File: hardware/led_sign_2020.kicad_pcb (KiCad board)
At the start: 2 copper layers, 70 x 86 mm, 29 parts, among them Q1 STD26P3LLH6, U1 ESP32-DevKitC, U2 MC74VHC1GT125, U3 MC74VHC1GT125, U4 MAX17601, U5 MAX17601, U6 MAX17601, U7 MAX17601

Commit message: no idea what I changed
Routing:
- net /DATA: track 14.3 -> 12.4 mm
- net /EN: track 79.0 -> 80.4 mm
- net /CLK: track 19.2 -> 18.5 mm
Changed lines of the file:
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@@
     (thickness 1.6)
     (drawings 10)
-    (tracks 367)
+    (tracks 364)
     (zones 0)
     (modules 29)
@@
   )
   (setup
-    (last_trace_width 2)
+    (last_trace_width 0.25)
     (user_trace_width 0.25)
     (user_trace_width 0.5)
@@
   (segment (start 120.1 75.4) (end 120.8 76.1) (width 0.25) (layer F.Cu) (net 1))
   (segment (start 118.4 75.4) (end 120.1 75.4) (width 0.25) (layer F.Cu) (net 1))
-  (segment (start 116.65 70.66) (end 116.65 70.15) (width 0.25) (layer F.Cu) (net 1))
-  (segment (start 120.384999 69.984999) (end 120.8 70.4) (width 0.25) (layer F.Cu) (net 1))
-  (segment (start 116.65 70.15) (end 116.815001 69.984999) (width 0.25) (layer F.Cu) (net 1))
-  (segment (start 118.55 70.66) (end 118.55 70.05) (width 0.25) (layer F.Cu) (net 1))
-  (segment (start 118.55 70.05) (end 118.484999 69.984999) (width 0.25) (layer F.Cu) (net 1))
-  (segment (start 118.484999 69.984999) (end 120.384999 69.984999) (width 0.25) (layer F.Cu) (net 1))
-  (segment (start 116.815001 69.984999) (end 118.484999 69.984999) (width 0.25) (layer F.Cu) (net 1))
   (via (at 119.8 76.9) (size 0.8) (drill 0.4) (layers F.Cu B.Cu) (net 1))
   (segment (start 120.6 76.1) (end 119.8 76.9) (width 0.25) (layer F.Cu) (net 1))
@@
   (segment (start 92.7875 76.9875) (end 92.7 76.9) (width 0.25) (layer F.Cu) (net 1))
   (segment (start 96.9 76.9) (end 92.7 76.9) (width 2) (layer B.Cu) (net 1))
-  (segment (start 81.94 79.659994) (end 81.94 84.06) (width 0.5) (layer F.Cu) (net 1))
-  (segment (start 81.94 84.06) (end 81.94 85.53) (width 0.5) (layer F.Cu) (net 1))
-  (segment (start 84.7 76.899994) (end 81.94 79.659994) (width 0.5) (layer F.Cu) (net 1))
+  (segment (start 81.94 79.659994) (end 81.94 84.06) (width 2) (layer F.Cu) (net 1))
+  (segment (start 81.94 84.06) (end 81.94 85.53) (width 2) (layer F.Cu) (net 1))
+  (segment (start 84.7 76.899994) (end 81.94 79.659994) (width 2) (layer F.Cu) (net 1))
   (segment (start 119.799987 76.899987) (end 119.8 76.9) (width 2) (layer B.Cu) (net 1))
   (segment (start 104.900013 76.899987) (end 119.799987 76.899987) (width 2) (layer B.Cu) (net 1))
@@
   (segment (start 114.96 101.66) (end 114.96 110.93) (width 2) (layer B.Cu) (net 1))
   (segment (start 111.6 98.3) (end 114.96 101.66) (width 2) (layer B.Cu) (net 1))
+  (segment (start 116.65 70.15) (end 117 69.8) (width 0.25) (layer F.Cu) (net 1))
+  (segment (start 117 69.8) (end 118.3 69.8) (width 0.25) (layer F.Cu) (net 1))
+  (segment (start 116.65 70.66) (end 116.65 70.15) (width 0.25) (layer F.Cu) (net 1))
+  (segment (start 118.669998 69.8) (end 120.2 69.8) (width 0.25) (layer F.Cu) (net 1))
+  (segment (start 118.55 69.919998) (end 118.669998 69.8) (width 0.25) (layer F.Cu) (net 1))
+  (segment (start 120.2 69.8) (end 120.8 70.4) (width 0.25) (layer F.Cu) (net 1))
+  (segment (start 118.55 70.66) (end 118.55 69.919998) (width 0.25) (layer F.Cu) (net 1))
+  (segment (start 118.3 69.8) (end 118.669998 69.8) (width 0.25) (layer F.Cu) (net 1))
   (segment (start 88.9 68.94) (end 88.94 68.9) (width 0.5) (layer F.Cu) (net 2))
   (via (at 112.9 66.1) (size 0.8) (drill 0.4) (layers F.Cu B.Cu) (net 2))
@@
   (segment (start 108.7 74.1) (end 108.7 68.9) (width 0.5) (layer B.Cu) (net 8))
   (segment (start 85 68.9) (end 108.7 68.9) (width 0.5) (layer B.Cu) (net 8))
-  (segment (start 108.7 68.9) (end 113.9 68.9) (width 0.5) (layer B.Cu) (net 8))
-  (via (at 115.5 65.8) (size 0.8) (drill 0.4) (layers F.Cu B.Cu) (net 8))
-  (segment (start 115.5 67.3) (end 115.5 65.8) (width 0.5) (layer B.Cu) (net 8))
-  (segment (start 113.9 68.9) (end 115.5 67.3) (width 0.5) (layer B.Cu) (net 8))
-  (segment (start 118.0125 65.8) (end 118.7 65.1125) (width 0.5) (layer F.Cu) (net 8))
-  (segment (start 115.5 65.8) (end 118.0125 65.8) (width 0.5) (layer F.Cu) (net 8))
   (segment (start 94.4 81.225) (end 94.675 81.5) (width 0.5) (layer F.Cu) (net 8))
   (segment (start 94.4 74.05) (end 94.4 81.225) (width 0.5) (layer F.Cu) (net 8))
   (segment (start 94.675 85.495) (end 94.64 85.53) (width 0.5) (layer F.Cu) (net 8))
   (segment (start 94.675 81.5) (end 94.675 85.495) (width 0.5) (layer F.Cu) (net 8))
+  (via (at 115.600008 64.7) (size 0.8) (drill 0.4) (layers F.Cu B.Cu) (net 8))
+  (segment (start 116.012508 65.1125) (end 115.600008 64.7) (width 0.5) (layer F.Cu) (net 8))
+  (segment (start 118.7 65.1125) (end 116.012508 65.1125) (width 0.5) (layer F.Cu) (net 8))
+  (segment (start 115.600008 68.099992) (end 115.600008 64.7) (width 0.5) (layer B.Cu) (net 8))
+  (segment (start 114.8 68.9) (end 115.600008 68.099992) (width 0.5) (layer B.Cu) (net 8))
+  (segment (start 108.7 68.9) (end 114.8 68.9) (width 0.5) (layer B.Cu) (net 8))
   (segment (start 121 65.125) (end 121 66.2) (width 0.25) (layer F.Cu) (net 9))
   (segment (start 121 66.2) (end 121 67) (width 0.25) (layer F.Cu) (net 9))
@@
   (segment (start 111.6 74.05) (end 111.6 75.9) (width 0.5) (layer F.Cu) (net 16))
   (via (at 117.1 72.6) (size 0.8) (drill 0.4) (layers F.Cu B.Cu) (net 17))
-  (segment (start 117.6 72.1) (end 117.1 72.6) (width 0.25) (layer F.Cu) (net 17))
-  (segment (start 117.6 70.66) (end 117.6 72.1) (width 0.25) (layer F.Cu) (net 17))
+  (segment (start 117.6 72.1) (end 117.1 72.6) (width 0.5) (layer F.Cu) (net 17))
+  (segment (start 117.6 70.66) (end 117.6 72.1) (width 0.5) (layer F.Cu) (net 17))
   (via (at 86.6 81.1) (size 0.8) (drill 0.4) (layers F.Cu B.Cu) (net 17))
   (segment (start 86.6 85.11) (end 86.6 81.1) (width 0.5) (layer F.Cu) (net 17))
   (segment (start 87.02 85.53) (end 86.6 85.11) (width 0.5) (layer F.Cu) (net 17))
   (segment (start 115.3 75.313782) (end 115.313792 75.29999) (width 0.25) (layer F.Cu) (net 17))
-  (segment (start 117.1 72.6) (end 115.313792 74.386208) (width 0.25) (layer B.Cu) (net 17))
+  (segment (start 117.1 72.6) (end 115.313792 74.386208) (width 0.5) (layer B.Cu) (net 17))
   (segment (start 86.6 81.1) (end 114.200002 81.1) (width 0.5) (layer B.Cu) (net 17))
   (segment (start 115.313792 75.29999) (end 115.313792 75.299977) (width 0.25) (layer F.Cu) (net 17))
   (segment (start 114.5 76.113769) (end 114.5 80.800002) (width 0.5) (layer F.Cu) (net 17))
   (via (at 115.313792 75.299977) (size 0.8) (drill 0.4) (layers F.Cu B.Cu) (net 17))
-  (segment (start 115.313792 74.386208) (end 115.313792 75.299977) (width 0.25) (layer B.Cu) (net 17))
+  (segment (start 115.313792 74.386208) (end 115.313792 75.299977) (width 0.5) (layer B.Cu) (net 17))
   (segment (start 115.313792 75.299977) (end 114.5 76.113769) (width 0.5) (layer F.Cu) (net 17))
   (segment (start 114.200002 81.1) (end 114.5 80.800002) (width 0.5) (layer B.Cu) (net 17))
@@
   (segment (start 118.6 73.98) (end 118.6 72.6) (width 0.25) (layer F.Cu) (net 19))
   (via (at 118.6 72.6) (size 0.8) (drill 0.4) (layers F.Cu B.Cu) (net 19))
-  (segment (start 118.6 67.4) (end 119.3 66.7) (width 0.25) (layer B.Cu) (net 19))
-  (segment (start 118.6 72.6) (end 118.6 67.4) (width 0.25) (layer B.Cu) (net 19))
+  (segment (start 118.6 67.4) (end 119.3 66.7) (width 0.5) (layer B.Cu) (net 19))
+  (segment (start 118.6 72.6) (end 118.6 67.4) (width 0.5) (layer B.Cu) (net 19))
   (via (at 119.3 66.7) (size 0.8) (drill 0.4) (layers F.Cu B.Cu) (net 19))
-  (segment (start 114.8 66.7) (end 119.3 66.7) (width 0.25) (layer F.Cu) (net 19))
-  (segment (start 114.55001 66.45001) (end 114.8 66.7) (width 0.25) (layer F.Cu) (net 19))
-  (segment (start 114.55001 60.35001) (end 114.55001 66.45001) (width 0.25) (layer F.Cu) (net 19))
   (segment (start 114.1 59.9) (end 114.55001 60.35001) (width 0.25) (layer F.Cu) (net 19))
-  (segment (start 111.6 59.9) (end 111.6 64.4) (width 0.25) (layer F.Cu) (net 20))
-  (segment (start 111.6 64.4) (end 112.2 65) (width 0.25) (layer F.Cu) (net 20))
-  (segment (start 112.2 65) (end 113.4 65) (width 0.25) (layer F.Cu) (net 20))
-  (segment (start 113.4 65) (end 114.1 65.7) (width 0.25) (layer F.Cu) (net 20))
-  (segment (start 114.1 65.7) (end 114.1 67.1) (width 0.25) (layer F.Cu) (net 20))
-  (segment (start 114.1 67.1) (end 114.4 67.4) (width 0.25) (layer F.Cu) (net 20))
-  (segment (start 114.4 67.4) (end 118.3 67.4) (width 0.25) (layer F.Cu) (net 20))
-  (segment (start 118.55 67.65) (end 118.55 68.34) (width 0.25) (layer F.Cu) (net 20))
-  (segment (start 118.3 67.4) (end 118.55 67.65) (width 0.25) (layer F.Cu) (net 20))
+  (segment (start 115.476765 66.199989) (end 118.799989 66.199989) (width 0.5) (layer F.Cu) (net 19))
+  (segment (start 114.55001 60.35001) (end 114.55001 65.273234) (width 0.5) (layer F.Cu) (net 19))
+  (segment (start 114.55001 65.273234) (end 115.476765 66.199989) (width 0.5) (layer F.Cu) (net 19))
+  (segment (start 118.799989 66.199989) (end 119.3 66.7) (width 0.5) (layer F.Cu) (net 19))
+  (segment (start 117.11 66.9) (end 118.55 68.34) (width 0.5) (layer F.Cu) (net 20))
+  (segment (start 115.186812 66.9) (end 117.11 66.9) (width 0.5) (layer F.Cu) (net 20))
+  (segment (start 111.6 63.313188) (end 115.186812 66.9) (width 0.5) (layer F.Cu) (net 20))
+  (segment (start 111.6 59.9) (end 111.6 63.313188) (width 0.5) (layer F.Cu) (net 20))
   (segment (start 106.6 59.9) (end 106.6 62.8) (width 1) (layer F.Cu) (net 21))
   (segment (start 106.6 62.8) (end 108.7 64.9) (width 1) (layer F.Cu) (net 21))

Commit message: settings
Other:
- rule pad_to_mask_clearance: 0 -> 0.0508

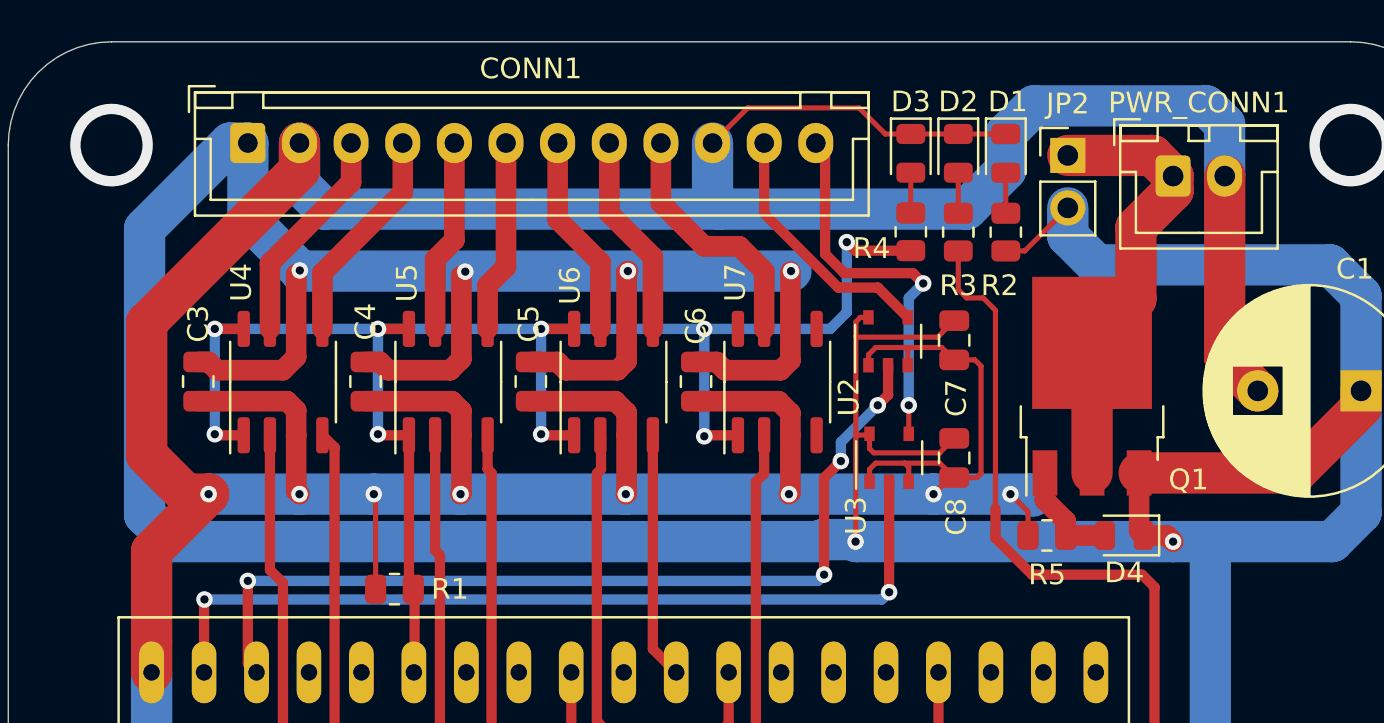
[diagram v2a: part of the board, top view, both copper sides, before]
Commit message: fix zener footprint
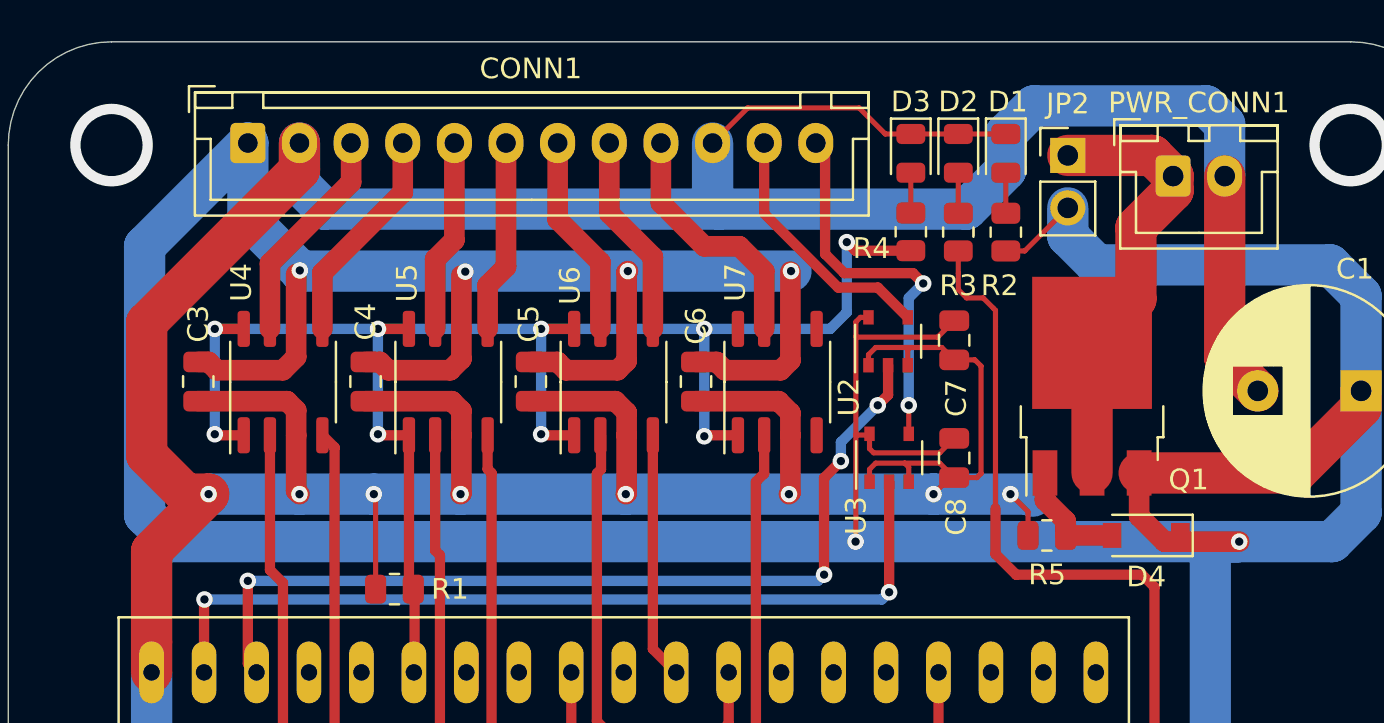
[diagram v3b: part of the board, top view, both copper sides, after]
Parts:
- D4: footprint Diode_SMD:D_0805_2012Metric -> Diode_SMD:D_SOD-123
- moved D4 1.06 mm to (130.1, 78.9)
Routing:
- net +5V: track 261.0 -> 266.0 mm

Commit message: add rediculous avatar and boost readme
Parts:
- added G***: LOGO, custom:breedx_avatar, F.Cu at (104.6, 127.1)
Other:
- board text added: "jason plumb :: noisybox.net - january 2021 https://github.com/breedx2/led_sign_2020"
- board text removed: "jason plumb :: noisybox.net - january 2021"
